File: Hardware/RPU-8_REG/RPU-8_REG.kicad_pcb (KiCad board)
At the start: 4 copper layers, 139.7 x 55.9 mm, 30 parts, among them J1 DATA_BUS, J2 ADDR_BUS, J3 CTRL_BUS, J4 Conn_01x03_Female, J5 REG_CTRL, J6 REG_BITS, U1 74HC245, U2 74HC245, U3 74HC377, U4 74HC377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

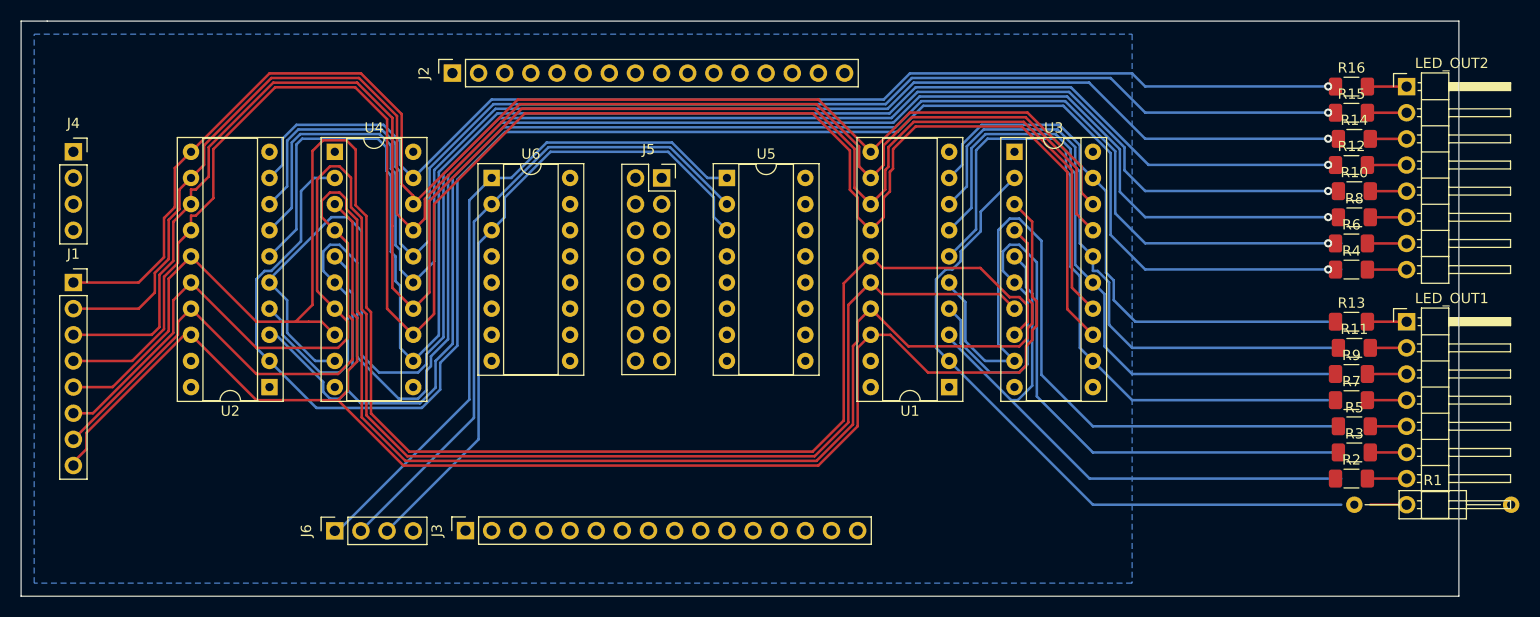
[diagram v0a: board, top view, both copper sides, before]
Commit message: fixed REG layout
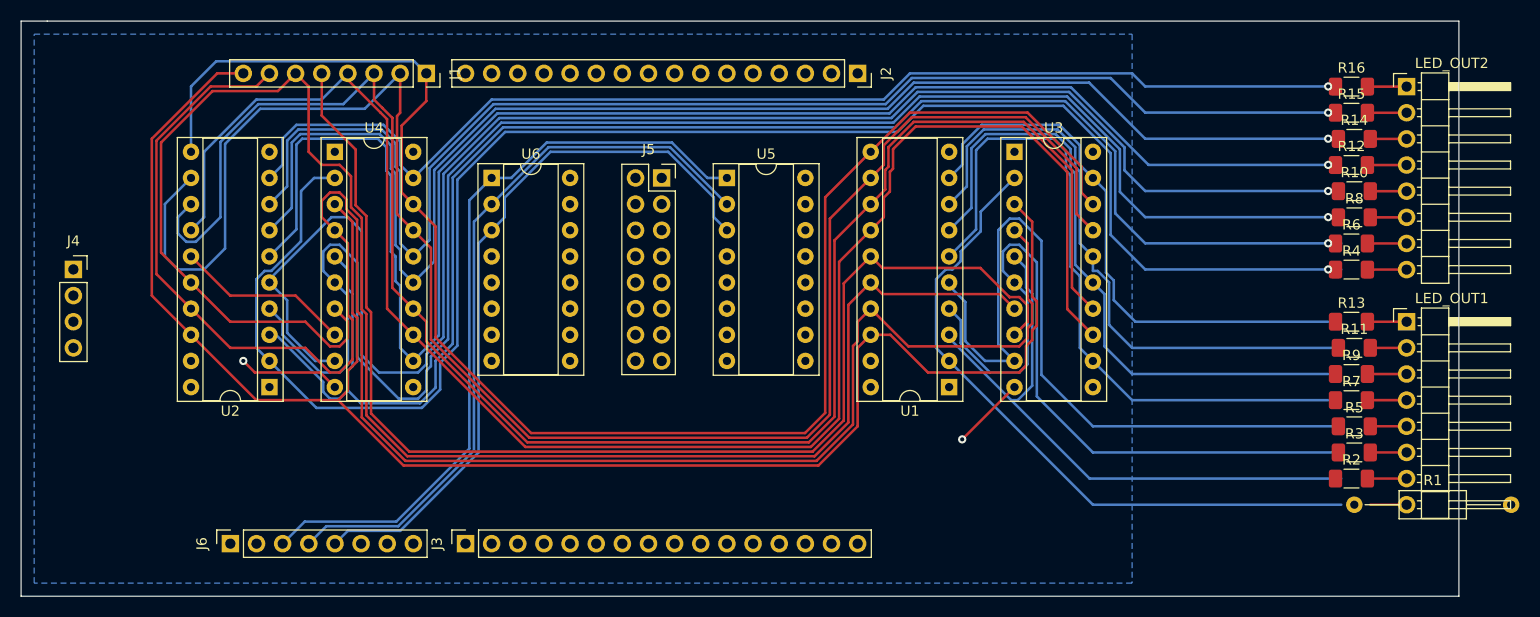
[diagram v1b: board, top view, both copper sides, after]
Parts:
- J6: value REG_BITS -> INST_BITS; footprint Connector_PinSocket_2.54mm:PinSocket_1x04_P2.54mm_Vertical -> Connector_PinSocket_2.54mm:PinSocket_1x08_P2.54mm_Vertical
- moved J1 39.9 mm to (153.7, 83.8), turned to -90 degrees
- moved J2 39.4 mm to (195.6, 83.8), turned to -90 degrees
- moved J4 11.4 mm to (119.4, 102.9)
- moved J6 10.2 mm to (134.6, 129.5)
- moved J3 1.27 mm to (157.5, 129.5)
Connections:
- J6 pad 1: INST_REG_0 -> INST0
- J6 pad 2: INST_REG_1 -> INST1
- J6 pad 3: INST_REG_2 -> INST2
- J6 pad 4: (no net) -> INST3
- U5 pad 1: INST_REG_0 -> INST2
- U5 pad 2: INST_REG_1 -> INST3
- U5 pad 3: INST_REG_2 -> INST4
- U6 pad 1: INST_REG_0 -> INST2
- U6 pad 2: INST_REG_1 -> INST3
- U6 pad 3: INST_REG_2 -> INST4
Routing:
- net INST2: track 0.00 -> 74.9 mm
- net INST3: track 0.00 -> 71.9 mm
- net INST4: track 0.00 -> 71.1 mm
- net INST_REG_0: track 66.5 -> 0.00 mm
- net INST_REG_2: track 64.8 -> 0.00 mm
- net INST_REG_1: track 64.5 -> 0.00 mm
- net D4: track 171.7 -> 138.5 mm
- net D1: track 146.6 -> 173.8 mm
- net D0: track 134.7 -> 156.8 mm
- net D3: track 185.5 -> 165.2 mm
- net GND: track 33.6 -> 17.1 mm, vias 0 -> 2
- net D7: track 153.5 -> 168.4 mm
- net CLK: track 170.0 -> 155.3 mm
- net D6: track 169.2 -> 183.0 mm
- net D5: track 160.8 -> 168.6 mm
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
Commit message: added images
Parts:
- R16: footprint Resistor_SMD:R_1206_3216Metric_Pad1.30x1.75mm_HandSolder -> Resistor_SMD:R_0402_1005Metric
- U3: footprint Package_DIP:DIP-20_W7.62mm_Socket -> Package_DIP:DIP-20_W7.62mm_SMDSocket_SmallPads
- moved U3 12.0 mm to (214.6, 102.9)

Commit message: add .readthedocs.yaml
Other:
- outline, holes or cut-outs redrawn
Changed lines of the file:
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@@
     )
   )
-  (gr_line (start 116.84 78.74) (end 254 78.74) (layer "Edge.Cuts") (width 0.1))
-  (gr_line (start 114.3 134.62) (end 114.3 78.74) (layer "Edge.Cuts") (width 0.1))
-  (gr_line (start 254 134.62) (end 114.3 134.62) (layer "Edge.Cuts") (width 0.1))
-  (gr_line (start 254 78.74) (end 254 134.62) (layer "Edge.Cuts") (width 0.1))
-  (gr_line (start 114.3 78.74) (end 116.84 78.74) (layer "Edge.Cuts") (width 0.1))
+  (gr_rect (start 114.3 78.74) (end 254 134.62) (layer "Edge.Cuts") (width 0.1) (fill none))
   (segment (start 153.67 83.82) (end 153.67 86.505) (width 0.25) (layer "F.Cu") (net 1))
   (segment (start 153.67 86.505) (end 151.275 88.9) (width 0.25) (layer "F.Cu") (net 1))
